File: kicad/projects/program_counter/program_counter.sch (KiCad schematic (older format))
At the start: 47 parts

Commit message: Program counter complete.
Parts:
- removed C? (x3): C, symbol Device:C
- removed D? (x8): LED, symbol Device:LED
- removed RN?: R_Network08_US, Resistor_THT:R_Array_SIP9, symbol Device:R_Network08_US
- removed U? (x3): 74HCT161, symbol eight-bit-computer:74HCT161
- added C5, C6, C7, C8, C9: 0.1uF, Capacitor_THT:C_Disc_D5.0mm_W2.5mm_P5.00mm, symbol Device:C
- added D1, D2, D3, D4, D5, D6, D7, D8: LED, eight-bit-computer:LED_D5.0mm_Horizontal_O3.81mm_Z3.0mm, symbol Device:LED
- added RN1: R_Network08_US, Resistor_THT:R_Array_SIP9, symbol Device:R_Network08_US
- added U5, U7, U9: 74HCT161, Package_DIP:DIP-16_W7.62mm, symbol eight-bit-computer:74HCT161
- C1, C2, C3, C4: renamed from C?; value C -> 0.1uF; footprint (none) -> Capacitor_THT:C_Disc_D5.0mm_W2.5mm_P5.00mm
- C10, C11, C12: renamed from C?; value CP -> 33uF; footprint (none) -> Capacitor_THT:CP_Radial_D6.3mm_P2.50mm
- D10, D11, D12, D13, D14, D15, D16, D9: renamed from D?; footprint (none) -> eight-bit-computer:LED_D5.0mm_Horizontal_O3.81mm_Z3.0mm
- J1: renamed from J?; footprint (none) -> Connector_PinSocket_2.54mm:PinSocket_1x16_P2.54mm_Horizontal
- J2: renamed from J?; footprint (none) -> eight-bit-computer:backplane-connector-single-row-annotated
- J3: renamed from J?; footprint (none) -> eight-bit-computer:bus-connection
- J4: renamed from J?; footprint (none) -> eight-bit-computer:aux-connection
- U1: renamed from U?; footprint (none) -> Package_DIP:DIP-14_W7.62mm
- U2, U4, U6, U8: renamed from U?; footprint (none) -> Package_DIP:DIP-20_W7.62mm
- U3: renamed from U?; footprint (none) -> Package_DIP:DIP-16_W7.62mm
- gave numbers to parts that had none: 1
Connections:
- net labels added: BUS_00, BUS_01, BUS_02, BUS_03, BUS_04, BUS_05, BUS_06, BUS_07, BUS_08, BUS_09, BUS_10, BUS_11, BUS_12, BUS_13, BUS_14, BUS_15, CTNT_00, CTNT_01, CTNT_02, CTNT_03, CTNT_04, CTNT_05, CTNT_06, CTNT_07, CTNT_08, CTNT_09, CTNT_10, CTNT_11, CTNT_12, CTNT_13, CTNT_14, CTNT_15, DATA_CLK, PC_COUNT, PC_IN, PC_OUT, RESET, ~PC_IN, ~PC_OUT, ~RESET
- wire segments 10 -> 232
- no-connect marks 0 -> 34
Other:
- moved on the sheet: C1, C10, C11, C12, C2, C3, C4, D10, D11, D12, D13, D14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

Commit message: Move kikad libs to sixteen bit location and update projects.
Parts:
- D1, D10, D11, D12, D13, D14, D15, D16, D2, D3, D4, D5, D6, D7, D8, D9: footprint eight-bit-computer:LED_D5.0mm_Horizontal_O3.81mm_Z3.0mm -> sixteen-bit-computer:LED_D5.0mm_Horizontal_O3.81mm_Z3.0mm
- J2: footprint eight-bit-computer:backplane-connector-single-row-annotated -> sixteen-bit-computer:backplane-connector-single-row-annotated; symbol eight-bit-computer:Control_signal_backplane -> sixteen-bit-computer:Control_signal_backplane
- J3: footprint eight-bit-computer:bus-connection -> sixteen-bit-computer:bus-connection; symbol eight-bit-computer:Bus_connection -> sixteen-bit-computer:Bus_connection
- J4: footprint eight-bit-computer:aux-connection -> sixteen-bit-computer:aux-connection; symbol eight-bit-computer:Aux_connection -> sixteen-bit-computer:Aux_connection
- U2, U4, U6, U8: symbol eight-bit-computer:74HCT245 -> sixteen-bit-computer:74HCT245
- U3, U5, U7, U9: symbol eight-bit-computer:74HCT161 -> sixteen-bit-computer:74HCT161
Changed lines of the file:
@@
 $EndDescr
 $Comp
-L eight-bit-computer:Bus_connection J3
+L sixteen-bit-computer:Bus_connection J3
 U 1 1 5FC9E485
 P 13300 5300
 F 0 "J3" H 13162 6225 50  0000 C CNN
 F 1 "Bus_connection" H 13162 6134 50  0000 C CNN
-F 2 "eight-bit-computer:bus-connection" H 13200 5700 50  0001 C CNN
+F 2 "sixteen-bit-computer:bus-connection" H 13200 5700 50  0001 C CNN
 F 3 "~" H 13200 5700 50  0001 C CNN
 	1    13300 5300
@@
 $EndComp
 $Comp
-L eight-bit-computer:Control_signal_backplane J2
+L sixteen-bit-computer:Control_signal_backplane J2
 U 1 1 5FCA04A9
 P 12250 6000
 F 0 "J2" H 12137 7725 50  0000 C CNN
 F 1 "Control_signal_backplane" H 12137 7634 50  0000 C CNN
-F 2 "eight-bit-computer:backplane-connector-single-row-annotated" H 12250 6000 50  0001 C CNN
+F 2 "sixteen-bit-computer:backplane-connector-single-row-annotated" H 12250 6000 50  0001 C CNN
 F 3 "~" H 12250 6000 50  0001 C CNN
 	1    12250 6000
@@
 $EndComp
 $Comp
-L eight-bit-computer:74HCT245 U6
+L sixteen-bit-computer:74HCT245 U6
 U 1 1 5FCA6309
 P 5800 6000
@@
 $EndComp
 $Comp
-L eight-bit-computer:74HCT245 U4
+L sixteen-bit-computer:74HCT245 U4
 U 1 1 5FCA733A
 P 3700 6000
@@
 $EndComp
 $Comp
-L eight-bit-computer:74HCT245 U2
+L sixteen-bit-computer:74HCT245 U2
 U 1 1 5FCAF774
 P 2450 9250
@@
 $EndComp
 $Comp
-L eight-bit-computer:74HCT245 U8
+L sixteen-bit-computer:74HCT245 U8
 U 1 1 5FCAFEA6
 P 6950 9250
@@
 F 0 "D16" H 7800 8600 50  0000 C CNN
 F 1 "LED" H 7650 8600 50  0000 C CNN
-F 2 "eight-bit-computer:LED_D5.0mm_Horizontal_O3.81mm_Z3.0mm" H 8050 8650 50  0001 C CNN
+F 2 "sixteen-bit-computer:LED_D5.0mm_Horizontal_O3.81mm_Z3.0mm" H 8050 8650 50  0001 C CNN
 F 3 "~" H 8050 8650 50  0001 C CNN
 	1    8050 8650
@@
 F 0 "D15" H 7800 8750 50  0000 C CNN
 F 1 "LED" H 7650 8750 50  0000 C CNN
-F 2 "eight-bit-computer:LED_D5.0mm_Horizontal_O3.81mm_Z3.0mm" H 8050 8800 50  0001 C CNN
+F 2 "sixteen-bit-computer:LED_D5.0mm_Horizontal_O3.81mm_Z3.0mm" H 8050 8800 50  0001 C CNN
 F 3 "~" H 8050 8800 50  0001 C CNN
 	1    8050 8800
@@
 F 0 "D14" H 7800 8900 50  0000 C CNN
 F 1 "LED" H 7650 8900 50  0000 C CNN
-F 2 "eight-bit-computer:LED_D5.0mm_Horizontal_O3.81mm_Z3.0mm" H 8050 8950 50  0001 C CNN
+F 2 "sixteen-bit-computer:LED_D5.0mm_Horizontal_O3.81mm_Z3.0mm" H 8050 8950 50  0001 C CNN
 F 3 "~" H 8050 8950 50  0001 C CNN
 	1    8050 8950
@@
 F 0 "D13" H 7800 9050 50  0000 C CNN
 F 1 "LED" H 7650 9050 50  0000 C CNN
-F 2 "eight-bit-computer:LED_D5.0mm_Horizontal_O3.81mm_Z3.0mm" H 8050 9100 50  0001 C CNN
+F 2 "sixteen-bit-computer:LED_D5.0mm_Horizontal_O3.81mm_Z3.0mm" H 8050 9100 50  0001 C CNN
 F 3 "~" H 8050 9100 50  0001 C CNN
 	1    8050 9100
@@
 F 0 "D12" H 7800 9200 50  0000 C CNN
 F 1 "LED" H 7650 9200 50  0000 C CNN
-F 2 "eight-bit-computer:LED_D5.0mm_Horizontal_O3.81mm_Z3.0mm" H 8050 9250 50  0001 C CNN
+F 2 "sixteen-bit-computer:LED_D5.0mm_Horizontal_O3.81mm_Z3.0mm" H 8050 9250 50  0001 C CNN
 F 3 "~" H 8050 9250 50  0001 C CNN
 	1    8050 9250
@@
 F 0 "D11" H 7800 9350 50  0000 C CNN
 F 1 "LED" H 7650 9350 50  0000 C CNN
-F 2 "eight-bit-computer:LED_D5.0mm_Horizontal_O3.81mm_Z3.0mm" H 8050 9400 50  0001 C CNN
+F 2 "sixteen-bit-computer:LED_D5.0mm_Horizontal_O3.81mm_Z3.0mm" H 8050 9400 50  0001 C CNN
 F 3 "~" H 8050 9400 50  0001 C CNN
 	1    8050 9400
@@
 F 0 "D10" H 7800 9500 50  0000 C CNN
 F 1 "LED" H 7650 9500 50  0000 C CNN
-F 2 "eight-bit-computer:LED_D5.0mm_Horizontal_O3.81mm_Z3.0mm" H 8050 9550 50  0001 C CNN
+F 2 "sixteen-bit-computer:LED_D5.0mm_Horizontal_O3.81mm_Z3.0mm" H 8050 9550 50  0001 C CNN
 F 3 "~" H 8050 9550 50  0001 C CNN
 	1    8050 9550
@@
 F 0 "D9" H 7800 9650 50  0000 C CNN
 F 1 "LED" H 7650 9650 50  0000 C CNN
-F 2 "eight-bit-computer:LED_D5.0mm_Horizontal_O3.81mm_Z3.0mm" H 8050 9700 50  0001 C CNN
+F 2 "sixteen-bit-computer:LED_D5.0mm_Horizontal_O3.81mm_Z3.0mm" H 8050 9700 50  0001 C CNN
 F 3 "~" H 8050 9700 50  0001 C CNN
 	1    8050 9700
@@
 $EndComp
 $Comp
-L eight-bit-computer:74HCT161 U3
+L sixteen-bit-computer:74HCT161 U3
 U 1 1 5FCA368E
 P 3200 2450
@@
 $EndComp
 $Comp
-L eight-bit-computer:74HCT161 U5
+L sixteen-bit-computer:74HCT161 U5
 U 1 1 5FD16858
 P 5050 2450
@@
 $EndComp
 $Comp
-L eight-bit-computer:74HCT161 U7
+L sixteen-bit-computer:74HCT161 U7
 U 1 1 5FD1A3E7
 P 6900 2450
@@
 $EndComp
 $Comp
-L eight-bit-computer:74HCT161 U9
+L sixteen-bit-computer:74HCT161 U9
 U 1 1 5FD1C8F3
 P 8750 2450
@@
 DATA_CLK
 $Comp
-L eight-bit-computer:Aux_connection J4
+L sixteen-bit-computer:Aux_connection J4
 U 1 1 5FC9DB32
 P 13300 7100
 F 0 "J4" H 13212 7725 50  0000 C CNN
 F 1 "Aux_connection" H 13212 7634 50  0000 C CNN
-F 2 "eight-bit-computer:aux-connection" H 13300 7100 50  0001 C CNN
+F 2 "sixteen-bit-computer:aux-connection" H 13300 7100 50  0001 C CNN
 F 3 "~" H 13300 7100 50  0001 C CNN
 	1    13300 7100
@@
 F 0 "D8" H 3300 8600 50  0000 C CNN
 F 1 "LED" H 3150 8600 50  0000 C CNN
-F 2 "eight-bit-computer:LED_D5.0mm_Horizontal_O3.81mm_Z3.0mm" H 3550 8650 50  0001 C CNN
+F 2 "sixteen-bit-computer:LED_D5.0mm_Horizontal_O3.81mm_Z3.0mm" H 3550 8650 50  0001 C CNN
 F 3 "~" H 3550 8650 50  0001 C CNN
 	1    3550 8650
@@
 F 0 "D7" H 3300 8750 50  0000 C CNN
 F 1 "LED" H 3150 8750 50  0000 C CNN
-F 2 "eight-bit-computer:LED_D5.0mm_Horizontal_O3.81mm_Z3.0mm" H 3550 8800 50  0001 C CNN
+F 2 "sixteen-bit-computer:LED_D5.0mm_Horizontal_O3.81mm_Z3.0mm" H 3550 8800 50  0001 C CNN
 F 3 "~" H 3550 8800 50  0001 C CNN
 	1    3550 8800
@@
 F 0 "D6" H 3300 8900 50  0000 C CNN
 F 1 "LED" H 3150 8900 50  0000 C CNN
-F 2 "eight-bit-computer:LED_D5.0mm_Horizontal_O3.81mm_Z3.0mm" H 3550 8950 50  0001 C CNN
+F 2 "sixteen-bit-computer:LED_D5.0mm_Horizontal_O3.81mm_Z3.0mm" H 3550 8950 50  0001 C CNN
 F 3 "~" H 3550 8950 50  0001 C CNN
 	1    3550 8950
@@
 F 0 "D5" H 3300 9050 50  0000 C CNN
 F 1 "LED" H 3150 9050 50  0000 C CNN
-F 2 "eight-bit-computer:LED_D5.0mm_Horizontal_O3.81mm_Z3.0mm" H 3550 9100 50  0001 C CNN
+F 2 "sixteen-bit-computer:LED_D5.0mm_Horizontal_O3.81mm_Z3.0mm" H 3550 9100 50  0001 C CNN
 F 3 "~" H 3550 9100 50  0001 C CNN
 	1    3550 9100
@@
 F 0 "D4" H 3300 9200 50  0000 C CNN
 F 1 "LED" H 3150 9200 50  0000 C CNN
-F 2 "eight-bit-computer:LED_D5.0mm_Horizontal_O3.81mm_Z3.0mm" H 3550 9250 50  0001 C CNN
+F 2 "sixteen-bit-computer:LED_D5.0mm_Horizontal_O3.81mm_Z3.0mm" H 3550 9250 50  0001 C CNN
 F 3 "~" H 3550 9250 50  0001 C CNN
 	1    3550 9250
@@
 F 0 "D3" H 3300 9350 50  0000 C CNN
 F 1 "LED" H 3150 9350 50  0000 C CNN
-F 2 "eight-bit-computer:LED_D5.0mm_Horizontal_O3.81mm_Z3.0mm" H 3550 9400 50  0001 C CNN
+F 2 "sixteen-bit-computer:LED_D5.0mm_Horizontal_O3.81mm_Z3.0mm" H 3550 9400 50  0001 C CNN
 F 3 "~" H 3550 9400 50  0001 C CNN
 	1    3550 9400
@@
 F 0 "D2" H 3300 9500 50  0000 C CNN
 F 1 "LED" H 3150 9500 50  0000 C CNN
-F 2 "eight-bit-computer:LED_D5.0mm_Horizontal_O3.81mm_Z3.0mm" H 3550 9550 50  0001 C CNN
+F 2 "sixteen-bit-computer:LED_D5.0mm_Horizontal_O3.81mm_Z3.0mm" H 3550 9550 50  0001 C CNN
 F 3 "~" H 3550 9550 50  0001 C CNN
 	1    3550 9550
@@
 F 0 "D1" H 3300 9650 50  0000 C CNN
 F 1 "LED" H 3150 9650 50  0000 C CNN
-F 2 "eight-bit-computer:LED_D5.0mm_Horizontal_O3.81mm_Z3.0mm" H 3550 9700 50  0001 C CNN
+F 2 "sixteen-bit-computer:LED_D5.0mm_Horizontal_O3.81mm_Z3.0mm" H 3550 9700 50  0001 C CNN
 F 3 "~" H 3550 9700 50  0001 C CNN
 	1    3550 9700

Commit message: Switch to HC series chips and fix some labelling in program counter or register PCB.
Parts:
- U1: value 74HCT04 -> 74HC04; symbol 74xx:74HCT04 -> 74xx:74HC04
- U2, U4, U6, U8: value 74HCT245 -> 74HC245; symbol sixteen-bit-computer:74HCT245 -> sixteen-bit-computer:74HC245
- U3, U5, U7, U9: value 74HCT161 -> 74HC161; symbol sixteen-bit-computer:74HCT161 -> sixteen-bit-computer:74HC161
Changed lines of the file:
@@
 $EndComp
 $Comp
-L sixteen-bit-computer:74HCT245 U6
+L sixteen-bit-computer:74HC245 U6
 U 1 1 5FCA6309
 P 5800 6000
 F 0 "U6" H 5550 6700 50  0000 C CNN
-F 1 "74HCT245" H 6050 6700 50  0000 C CNN
+F 1 "74HC245" H 6050 6700 50  0000 C CNN
 F 2 "Package_DIP:DIP-20_W7.62mm" H 5450 6000 50  0001 C CNN
 F 3 "" H 5450 6000 50  0001 C CNN
@@
 $EndComp
 $Comp
-L sixteen-bit-computer:74HCT245 U4
+L sixteen-bit-computer:74HC245 U4
 U 1 1 5FCA733A
 P 3700 6000
 F 0 "U4" H 3500 6700 50  0000 C CNN
-F 1 "74HCT245" H 3950 6700 50  0000 C CNN
+F 1 "74HC245" H 3950 6700 50  0000 C CNN
 F 2 "Package_DIP:DIP-20_W7.62mm" H 3350 6000 50  0001 C CNN
 F 3 "" H 3350 6000 50  0001 C CNN
@@
 $EndComp
 $Comp
-L 74xx:74HCT04 U1
+L 74xx:74HC04 U1
 U 1 1 5FCA7FA7
 P 1400 3100
 F 0 "U1" H 1400 3417 50  0000 C CNN
-F 1 "74HCT04" H 1400 3326 50  0000 C CNN
+F 1 "74HC04" H 1400 3326 50  0000 C CNN
 F 2 "Package_DIP:DIP-14_W7.62mm" H 1400 3100 50  0001 C CNN
 F 3 "https://assets.nexperia.com/documents/data-sheet/74HC_HCT04.pdf" H 1400 3100 50  0001 C CNN
@@
 $EndComp
 $Comp
-L 74xx:74HCT04 U1
+L 74xx:74HC04 U1
 U 2 1 5FCA89A6
 P 1400 3650
 F 0 "U1" H 1400 3967 50  0000 C CNN
-F 1 "74HCT04" H 1400 3876 50  0000 C CNN
+F 1 "74HC04" H 1400 3876 50  0000 C CNN
 F 2 "Package_DIP:DIP-14_W7.62mm" H 1400 3650 50  0001 C CNN
 F 3 "https://assets.nexperia.com/documents/data-sheet/74HC_HCT04.pdf" H 1400 3650 50  0001 C CNN
@@
 $EndComp
 $Comp
-L 74xx:74HCT04 U1
+L 74xx:74HC04 U1
 U 3 1 5FCA9DFB
 P 1700 5450
 F 0 "U1" H 1700 5767 50  0000 C CNN
-F 1 "74HCT04" H 1700 5676 50  0000 C CNN
+F 1 "74HC04" H 1700 5676 50  0000 C CNN
 F 2 "Package_DIP:DIP-14_W7.62mm" H 1700 5450 50  0001 C CNN
 F 3 "https://assets.nexperia.com/documents/data-sheet/74HC_HCT04.pdf" H 1700 5450 50  0001 C CNN
@@
 $EndComp
 $Comp
-L 74xx:74HCT04 U1
+L 74xx:74HC04 U1
 U 4 1 5FCAA994
 P 12500 1850
 F 0 "U1" H 12500 2167 50  0000 C CNN
-F 1 "74HCT04" H 12500 2076 50  0000 C CNN
+F 1 "74HC04" H 12500 2076 50  0000 C CNN
 F 2 "Package_DIP:DIP-14_W7.62mm" H 12500 1850 50  0001 C CNN
 F 3 "https://assets.nexperia.com/documents/data-sheet/74HC_HCT04.pdf" H 12500 1850 50  0001 C CNN
@@
 $EndComp
 $Comp
-L 74xx:74HCT04 U1
+L 74xx:74HC04 U1
 U 5 1 5FCABCA3
 P 12500 2400
 F 0 "U1" H 12500 2717 50  0000 C CNN
-F 1 "74HCT04" H 12500 2626 50  0000 C CNN
+F 1 "74HC04" H 12500 2626 50  0000 C CNN
 F 2 "Package_DIP:DIP-14_W7.62mm" H 12500 2400 50  0001 C CNN
 F 3 "https://assets.nexperia.com/documents/data-sheet/74HC_HCT04.pdf" H 12500 2400 50  0001 C CNN
@@
 $EndComp
 $Comp
-L 74xx:74HCT04 U1
+L 74xx:74HC04 U1
 U 6 1 5FCAC5E4
 P 12500 2950
 F 0 "U1" H 12500 3267 50  0000 C CNN
-F 1 "74HCT04" H 12500 3176 50  0000 C CNN
+F 1 "74HC04" H 12500 3176 50  0000 C CNN
 F 2 "Package_DIP:DIP-14_W7.62mm" H 12500 2950 50  0001 C CNN
 F 3 "https://assets.nexperia.com/documents/data-sheet/74HC_HCT04.pdf" H 12500 2950 50  0001 C CNN
@@
 $EndComp
 $Comp
-L 74xx:74HCT04 U1
+L 74xx:74HC04 U1
 U 7 1 5FCAD347
 P 11500 2450
 F 0 "U1" H 11730 2496 50  0000 L CNN
-F 1 "74HCT04" H 11730 2405 50  0000 L CNN
+F 1 "74HC04" H 11730 2405 50  0000 L CNN
 F 2 "Package_DIP:DIP-14_W7.62mm" H 11500 2450 50  0001 C CNN
 F 3 "https://assets.nexperia.com/documents/data-sheet/74HC_HCT04.pdf" H 11500 2450 50  0001 C CNN
@@
 $EndComp
 $Comp
-L sixteen-bit-computer:74HCT245 U2
+L sixteen-bit-computer:74HC245 U2
 U 1 1 5FCAF774
 P 2450 9250
 F 0 "U2" H 2250 9950 50  0000 C CNN
-F 1 "74HCT245" H 2700 9950 50  0000 C CNN
+F 1 "74HC245" H 2700 9950 50  0000 C CNN
 F 2 "Package_DIP:DIP-20_W7.62mm" H 2100 9250 50  0001 C CNN
 F 3 "" H 2100 9250 50  0001 C CNN
@@
 $EndComp
 $Comp
-L sixteen-bit-computer:74HCT245 U8
+L sixteen-bit-computer:74HC245 U8
 U 1 1 5FCAFEA6
 P 6950 9250
 F 0 "U8" H 6750 9950 50  0000 C CNN
-F 1 "74HCT245" H 7200 9950 50  0000 C CNN
+F 1 "74HC245" H 7200 9950 50  0000 C CNN
 F 2 "Package_DIP:DIP-20_W7.62mm" H 6600 9250 50  0001 C CNN
 F 3 "" H 6600 9250 50  0001 C CNN
@@
 $EndComp
 $Comp
-L sixteen-bit-computer:74HCT161 U3
+L sixteen-bit-computer:74HC161 U3
 U 1 1 5FCA368E
 P 3200 2450
 F 0 "U3" H 2950 3100 50  0000 C CNN
-F 1 "74HCT161" H 3450 3100 50  0000 C CNN
+F 1 "74HC161" H 3450 3100 50  0000 C CNN
 F 2 "Package_DIP:DIP-16_W7.62mm" H 3200 2450 50  0001 C CNN
 F 3 "https://www.ti.com/lit/ds/symlink/cd54hc163.pdf" H 3200 2450 50  0001 C CNN
@@
 $EndComp
 $Comp
-L sixteen-bit-computer:74HCT161 U5
+L sixteen-bit-computer:74HC161 U5
 U 1 1 5FD16858
 P 5050 2450
 F 0 "U5" H 4800 3100 50  0000 C CNN
-F 1 "74HCT161" H 5300 3100 50  0000 C CNN
+F 1 "74HC161" H 5300 3100 50  0000 C CNN
 F 2 "Package_DIP:DIP-16_W7.62mm" H 5050 2450 50  0001 C CNN
 F 3 "https://www.ti.com/lit/ds/symlink/cd54hc163.pdf" H 5050 2450 50  0001 C CNN
@@
 $EndComp
 $Comp
-L sixteen-bit-computer:74HCT161 U7
+L sixteen-bit-computer:74HC161 U7
 U 1 1 5FD1A3E7
 P 6900 2450
 F 0 "U7" H 6650 3100 50  0000 C CNN
-F 1 "74HCT161" H 7150 3100 50  0000 C CNN
+F 1 "74HC161" H 7150 3100 50  0000 C CNN
 F 2 "Package_DIP:DIP-16_W7.62mm" H 6900 2450 50  0001 C CNN
 F 3 "https://www.ti.com/lit/ds/symlink/cd54hc163.pdf" H 6900 2450 50  0001 C CNN
@@
 $EndComp
 $Comp
-L sixteen-bit-computer:74HCT161 U9
+L sixteen-bit-computer:74HC161 U9
 U 1 1 5FD1C8F3
 P 8750 2450
 F 0 "U9" H 8500 3100 50  0000 C CNN
-F 1 "74HCT161" H 9000 3100 50  0000 C CNN
+F 1 "74HC161" H 9000 3100 50  0000 C CNN
 F 2 "Package_DIP:DIP-16_W7.62mm" H 8750 2450 50  0001 C CNN
 F 3 "https://www.ti.com/lit/ds/symlink/cd54hc163.pdf" H 8750 2450 50  0001 C CNN

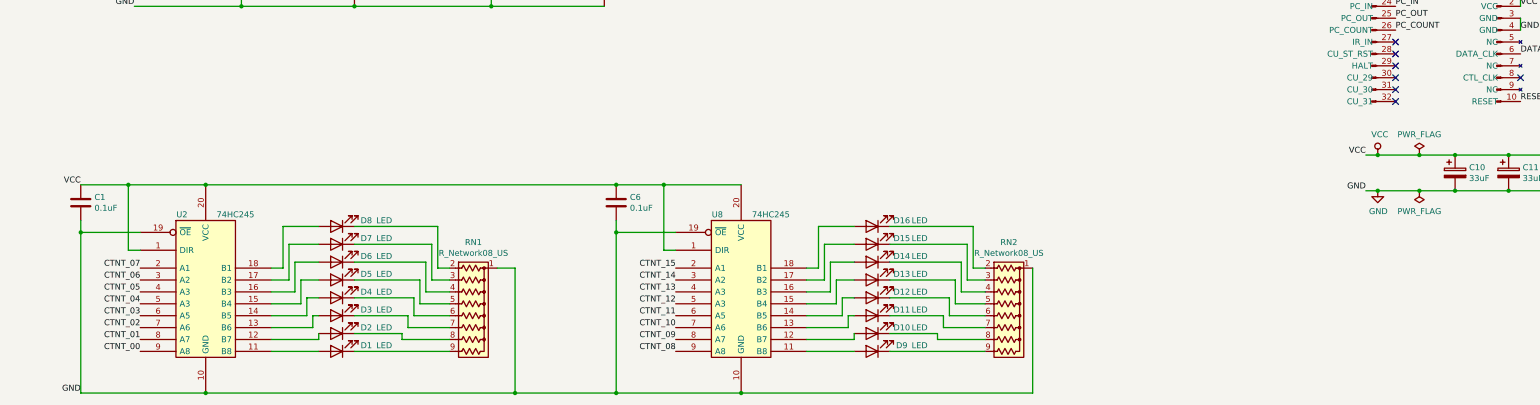
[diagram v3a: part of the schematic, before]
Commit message: Add top power and LED control to program counter.
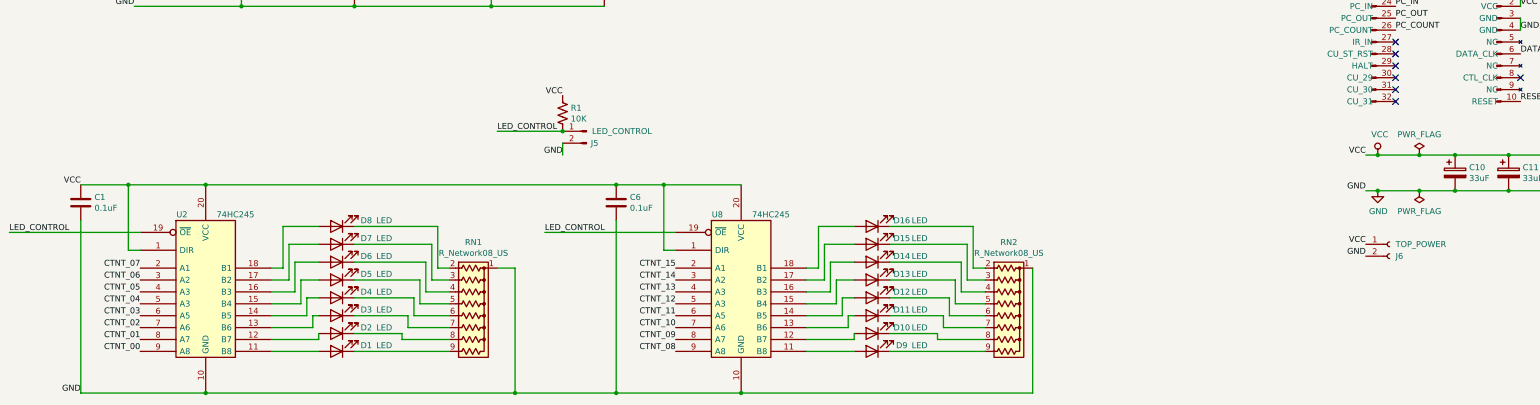
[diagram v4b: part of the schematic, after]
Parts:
- added J5: LED_CONTROL, Connector_PinHeader_2.54mm:PinHeader_1x02_P2.54mm_Horizontal, symbol Connector:Conn_01x02_Male
- added J6: TOP_POWER, Connector_PinSocket_2.54mm:PinSocket_1x02_P2.54mm_Horizontal, symbol Connector:Conn_01x02_Female
- added R1: 10K, Resistor_THT:R_Axial_DIN0207_L6.3mm_D2.5mm_P10.16mm_Horizontal, symbol Device:R_US
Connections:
- net GND: now also J5.2 (Pin_2), J6.2 (Pin_2); no longer U2.19 (~OE), U8.19 (~OE)
- net VCC: now also J6.1 (Pin_1), R1.1
- new net LED_CONTROL: J5.1 (Pin_1), R1.2, U2.19 (~OE), U8.19 (~OE)
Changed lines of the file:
@@
 	1400 8300 1800 8300
-Wire Wire Line
-	1400 8600 1400 8700
-Wire Wire Line
-	1900 8700 1400 8700
-Connection ~ 1400 8700
-Wire Wire Line
-	1400 8700 1400 10050
 Wire Wire Line
 	1900 8850 1800 8850
@@
 	6950 8300 6300 8300
 Wire Wire Line
-	5900 8600 5900 8700
-Wire Wire Line
 	5900 10050 6950 10050
 Wire Wire Line
@@
 Wire Wire Line
 	6300 8300 5900 8300
-Wire Wire Line
-	6400 8700 5900 8700
-Connection ~ 5900 8700
-Wire Wire Line
-	5900 8700 5900 10050
 Wire Wire Line
 	4050 1650 5050 1650
@@
 Wire Wire Line
 	3150 4950 2350 4950
+Text Label 12200 8800 2    50   ~ 0
+VCC
+Text Label 12200 8900 2    50   ~ 0
+GND
+Text Label 5450 7550 2    50   ~ 0
+VCC
+Text Label 5450 8050 2    50   ~ 0
+GND
+$Comp
+L Connector:Conn_01x02_Female J6
+U 1 1 62EB3B20
+P 12400 8800
+F 0 "J6" H 12450 8700 50  0000 L CNN
+F 1 "TOP_POWER" H 12450 8800 50  0000 L CNN
+F 2 "Connector_PinSocket_2.54mm:PinSocket_1x02_P2.54mm_Horizontal" H 12400 8800 50  0001 C CNN
+F 3 "~" H 12400 8800 50  0001 C CNN
+	1    12400 8800
+	1    0    0    -1
+$EndComp
+$Comp
+L Connector:Conn_01x02_Male J5
+U 1 1 62EB40E6
+P 5650 7850
+F 0 "J5" H 5550 7750 50  0000 L CNN
+F 1 "LED_CONTROL" H 5100 7850 50  0000 L CNN
+F 2 "Connector_PinHeader_2.54mm:PinHeader_1x02_P2.54mm_Horizontal" H 5650 7850 50  0001 C CNN
+F 3 "~" H 5650 7850 50  0001 C CNN
+	1    5650 7850
+	-1   0    0    -1
+$EndComp
+$Comp
+L Device:R_US R1
+U 1 1 62EEAC6F
+P 5450 7700
+F 0 "R1" H 5518 7746 50  0000 L CNN
+F 1 "10K" H 5518 7655 50  0000 L CNN
+F 2 "Resistor_THT:R_Axial_DIN0207_L6.3mm_D2.5mm_P10.16mm_Horizontal" V 5490 7690 50  0001 C CNN
+F 3 "~" H 5450 7700 50  0001 C CNN
+	1    5450 7700
+	1    0    0    -1
+$EndComp
+Connection ~ 5450 7850
+Text Label 4900 7850 0    50   ~ 0
+LED_CONTROL
+Wire Wire Line
+	5450 7950 5450 8050
+Wire Wire Line
+	4900 7850 5450 7850
+Wire Wire Line
+	1400 8600 1400 10050
+Wire Wire Line
+	5900 8600 5900 10050
+Text Label 5300 8700 0    50   ~ 0
+LED_CONTROL
+Text Label 800  8700 0    50   ~ 0
+LED_CONTROL
+Wire Wire Line
+	800  8700 1900 8700
+Wire Wire Line
+	5300 8700 6400 8700
 $EndSCHEMATC

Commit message: Add pullup on bus out on program counter and update LED control.
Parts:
- added R2: 10K, Resistor_THT:R_Axial_DIN0207_L6.3mm_D2.5mm_P10.16mm_Horizontal, symbol Device:R
- J5: footprint Connector_PinHeader_2.54mm:PinHeader_1x02_P2.54mm_Horizontal -> Connector_PinHeader_2.54mm:PinHeader_1x03_P2.54mm_Horizontal; symbol Connector:Conn_01x02_Male -> Connector:Conn_01x03_Male
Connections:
- net GND: now also J5.3 (Pin_3), R1.2; no longer J5.2 (Pin_2)
- net LED_CONTROL: now also J5.2 (Pin_2), R1.1; no longer J5.1 (Pin_1), R1.2
- net VCC: now also J5.1 (Pin_1), R2.2; no longer R1.1
- net ~PC_OUT: now also R2.1
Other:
- moved on the sheet: C2, C4, R1, U1C, U4, U6
